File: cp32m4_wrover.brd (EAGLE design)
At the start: 18 x 31.4 mm, 30 parts, among them Q3 DMG341, U2 AP2112-3.3, X2 32.768

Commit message: routing done-ish, ground airwires
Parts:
- removed R5: 330, microbuilder:0603-NO
- added SW1: SPST_TACT-KMR2, adafruit:KMR2
- moved R9 32.6 mm to (10.5, 6.86)
- moved C14 25.8 mm to (8.20, 8.55), turned to 180 degrees
- moved X2 25.8 mm to (8.12, 17.7)
- moved C4 23.6 mm to (8.06, 14.8), turned to 0 degrees
- moved C2 19.8 mm to (11.9, 19.8), turned to 0 degrees
- moved SJ1 16.4 mm to (9.02, 17.5), turned to 180 degrees
- moved LED2 3.27 mm to (21.0, 5.34), turned to 90 degrees
- moved C10 2.94 mm to (7.88, 12.3), turned to 270 degrees
- moved C11 2.67 mm to (21.4, 16.0), turned to 270 degrees
- moved C5 2.17 mm to (20.9, 8.00)
- moved R6 1.67 mm to (8.06, 20.6)
- moved U$43 0.51 mm to (9.98, 3.54)
- moved U$14 0.44 mm to (14.6, 13.7)
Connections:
- net !RESET: now also SW1.2, SW1.4; no longer R5.1
- net GND: now also SW1.1, SW1.3
- net RESET_SW: no longer R5.2
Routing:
- net +3V3: track 6.39 -> 64.1 mm, vias 0 -> 3
- net !RESET: track 1.71 -> 31.3 mm, vias 0 -> 3
- net D+: track 1.50 -> 25.3 mm, vias 1 -> 2
- net D-: track 1.35 -> 24.7 mm, vias 1 -> 2
- net SWCLK: track 0.00 -> 21.0 mm, vias 0 -> 3
- net SD2: track 0.00 -> 19.1 mm, vias 0 -> 1
- net CMD: track 0.00 -> 18.8 mm, vias 0 -> 1
- net SD3: track 0.00 -> 18.6 mm, vias 0 -> 1
- net SW5: track 0.00 -> 18.2 mm, vias 0 -> 1
- net BAT_VOLTAGE: track 0.00 -> 17.2 mm, vias 0 -> 1
- net QSPI_CS: track 0.00 -> 16.8 mm, vias 0 -> 2
- net SW3/4_DIV: track 0.00 -> 16.4 mm, vias 0 -> 1
- net SW1/2_DIV: track 0.00 -> 16.2 mm, vias 0 -> 1
- net VBAT: track 0.00 -> 14.7 mm, vias 0 -> 1
- net CLK: track 0.00 -> 14.4 mm, vias 0 -> 1
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- added copper zone on layer 1, net GND
- added copper zone on layer 16, net GND

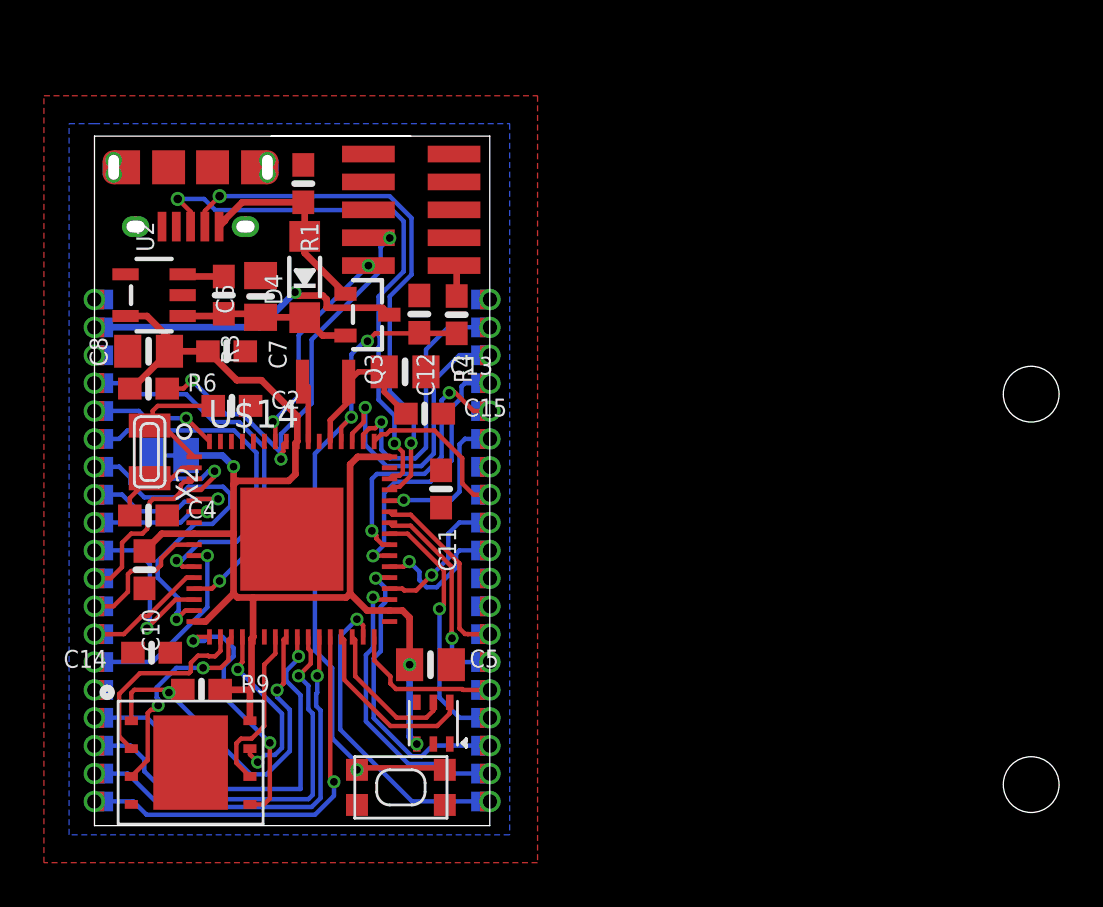
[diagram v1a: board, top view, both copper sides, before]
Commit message: major airwires fixed?
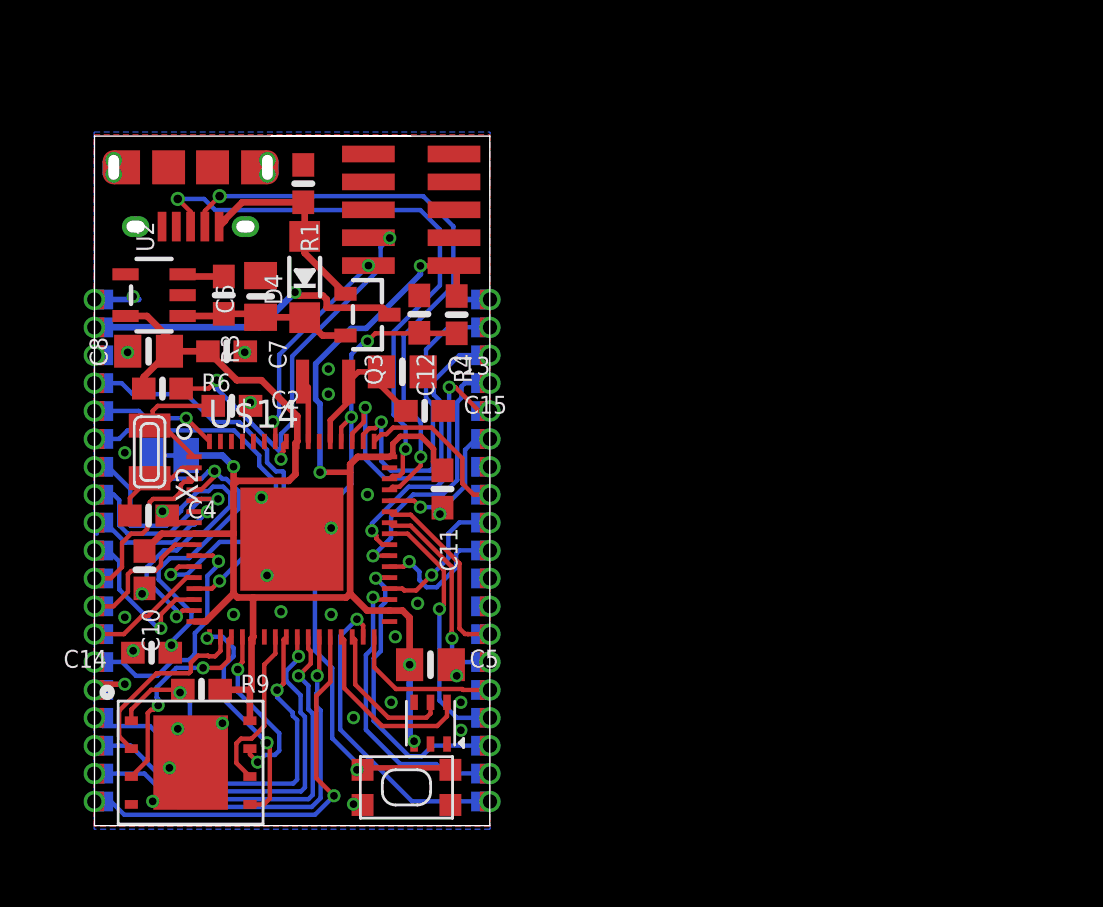
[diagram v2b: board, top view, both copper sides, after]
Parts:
- moved R6 0.63 mm to (8.70, 20.6)
- moved SW1 0.25 mm to (19.8, 2.41)
- moved C13 0.13 mm to (19.6, 21.3)
- moved C15 0.13 mm to (20.6, 19.6)
- moved LED2 0.13 mm to (20.9, 5.34)
- moved C11 0.06 mm to (21.5, 16.0)
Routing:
- net +3V3: track 64.1 -> 83.0 mm, vias 3 -> 5
- net GND: track 0.00 -> 17.0 mm, vias 0 -> 32
- net AREF: track 4.94 -> 16.8 mm, vias 1 -> 2
- net SW1/2_DIV: track 16.2 -> 18.5 mm
- net D-: track 24.7 -> 26.9 mm
- net QSPI_CS: track 16.8 -> 18.8 mm
- net EX_HDR_3_OR: track 9.13 -> 11.1 mm
- net SW3/4_DIV: track 16.4 -> 18.2 mm
- net VSPI_CS1: track 13.6 -> 15.4 mm
- net VSPI_MOSI: track 12.8 -> 14.6 mm
- net D+: track 25.3 -> 27.0 mm
- net SW10: track 7.31 -> 8.90 mm
- net QSPI_DATA[0]: track 11.9 -> 10.5 mm
- net SW9: track 5.96 -> 7.26 mm
- net BAT_VOLTAGE: track 17.2 -> 18.1 mm
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
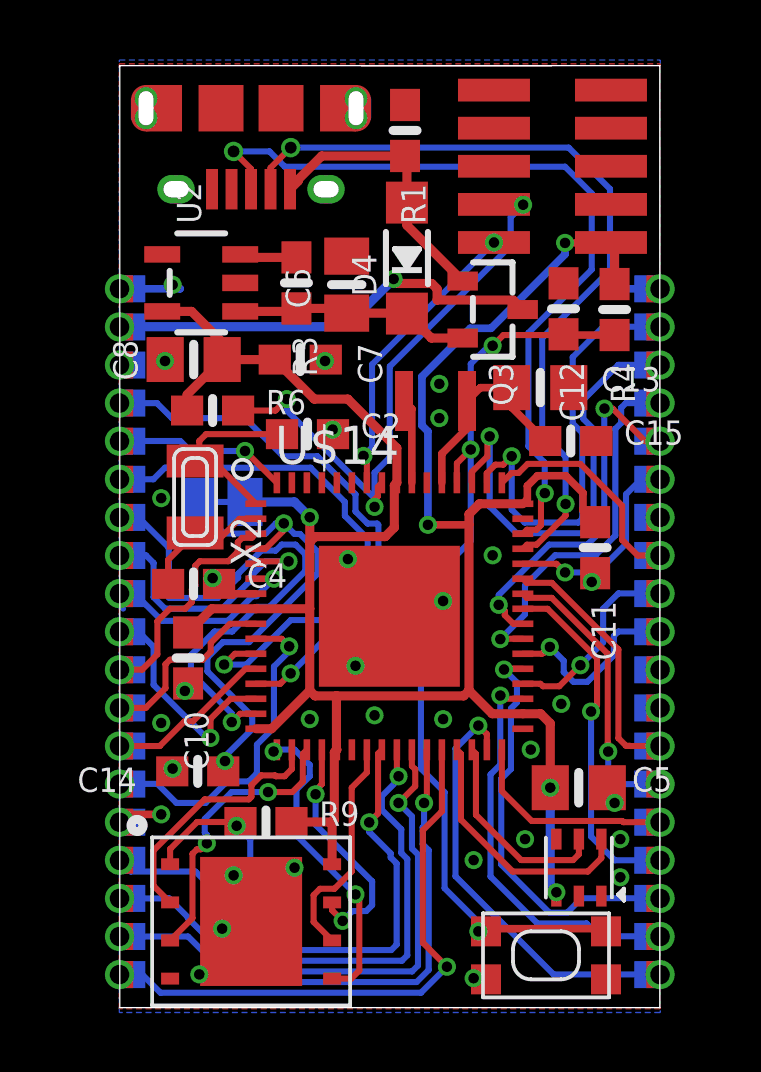
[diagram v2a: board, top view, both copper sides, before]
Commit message: all DRCs resolved
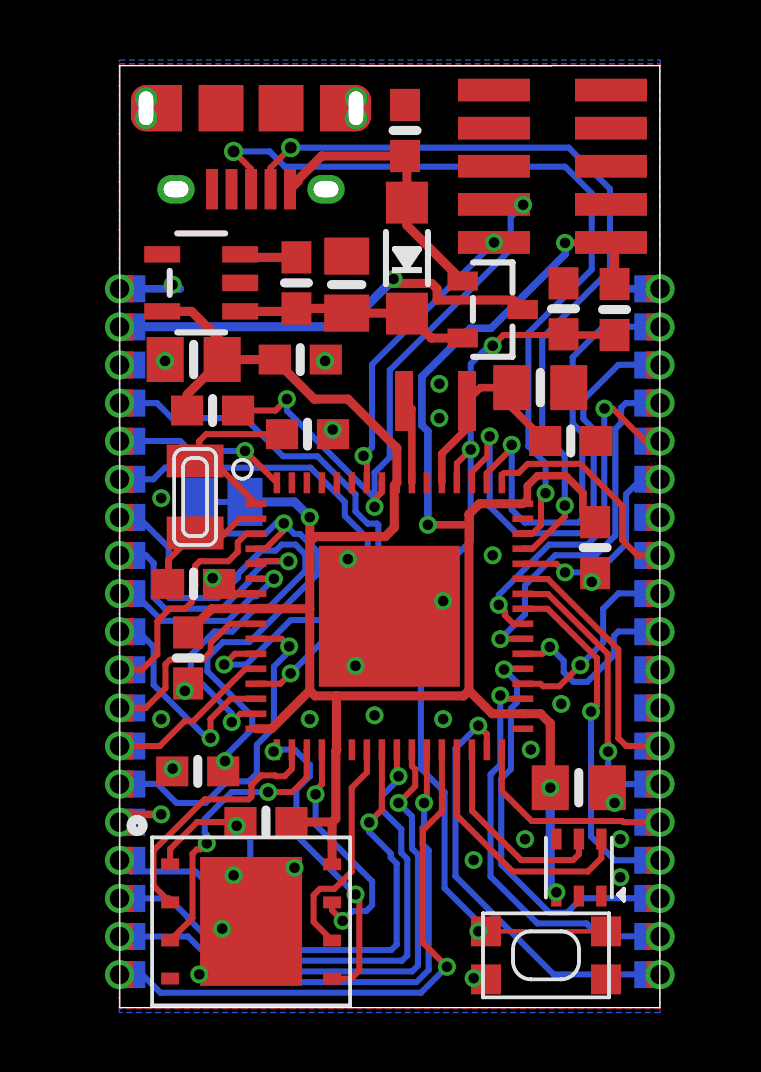
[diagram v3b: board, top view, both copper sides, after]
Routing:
- net VSPI_MOSI: track 14.6 -> 15.2 mm
- net SW9: track 7.26 -> 6.71 mm
